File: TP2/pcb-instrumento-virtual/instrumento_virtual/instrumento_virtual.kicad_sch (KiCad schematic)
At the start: 29 parts

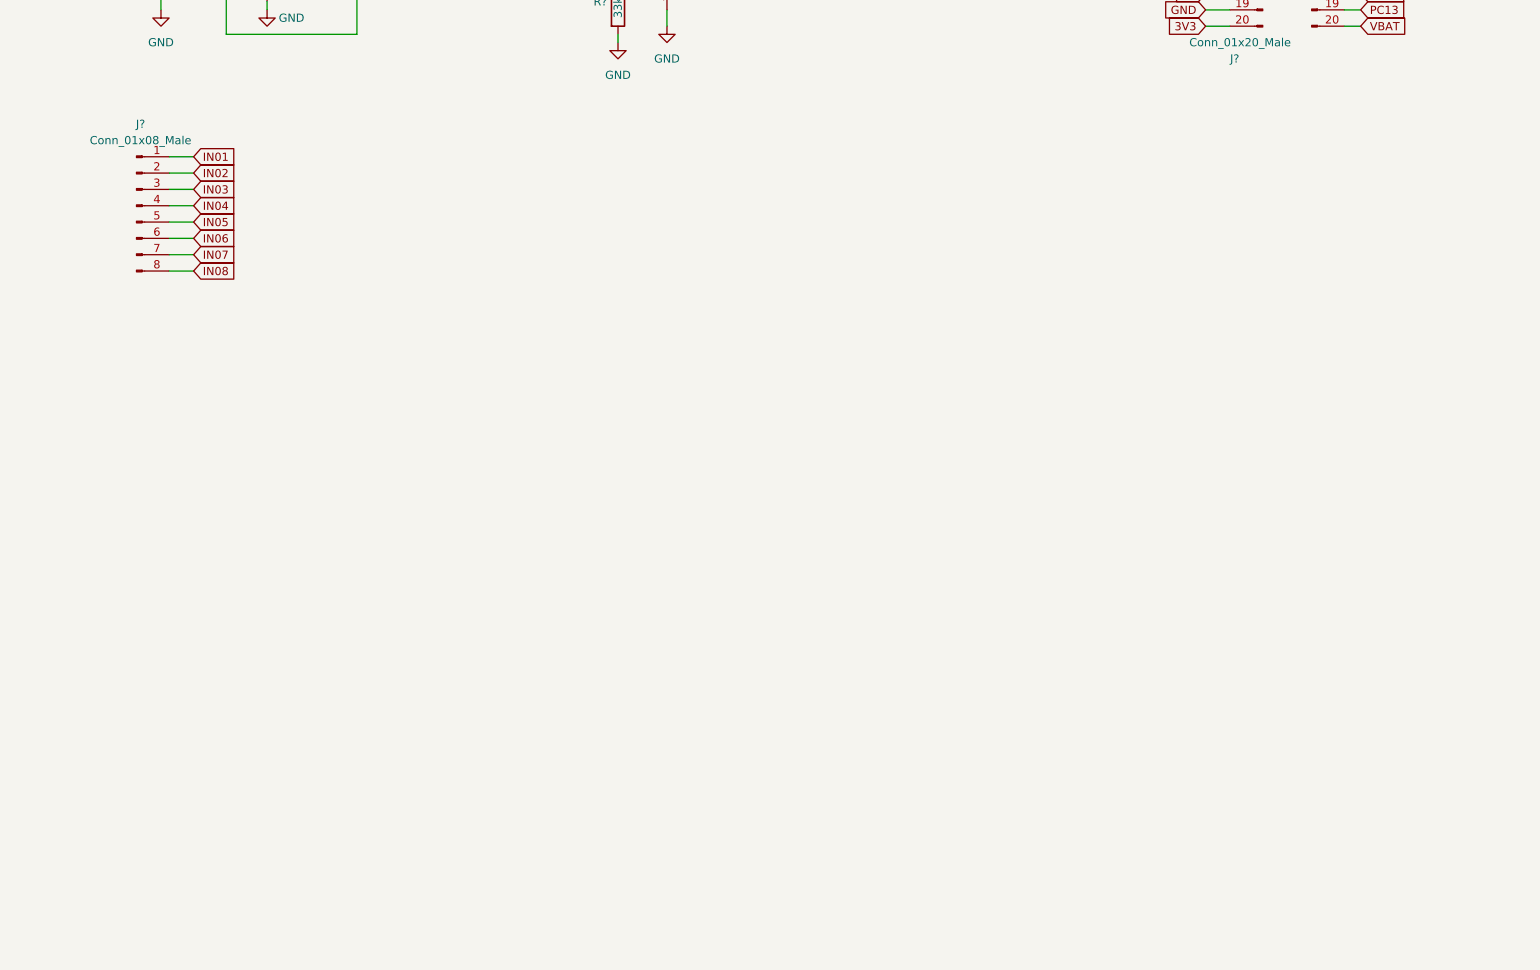
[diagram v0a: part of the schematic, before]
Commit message: agrega etapas de operacionales de entradas y circuitos de protección con clamping diodes en la pcb
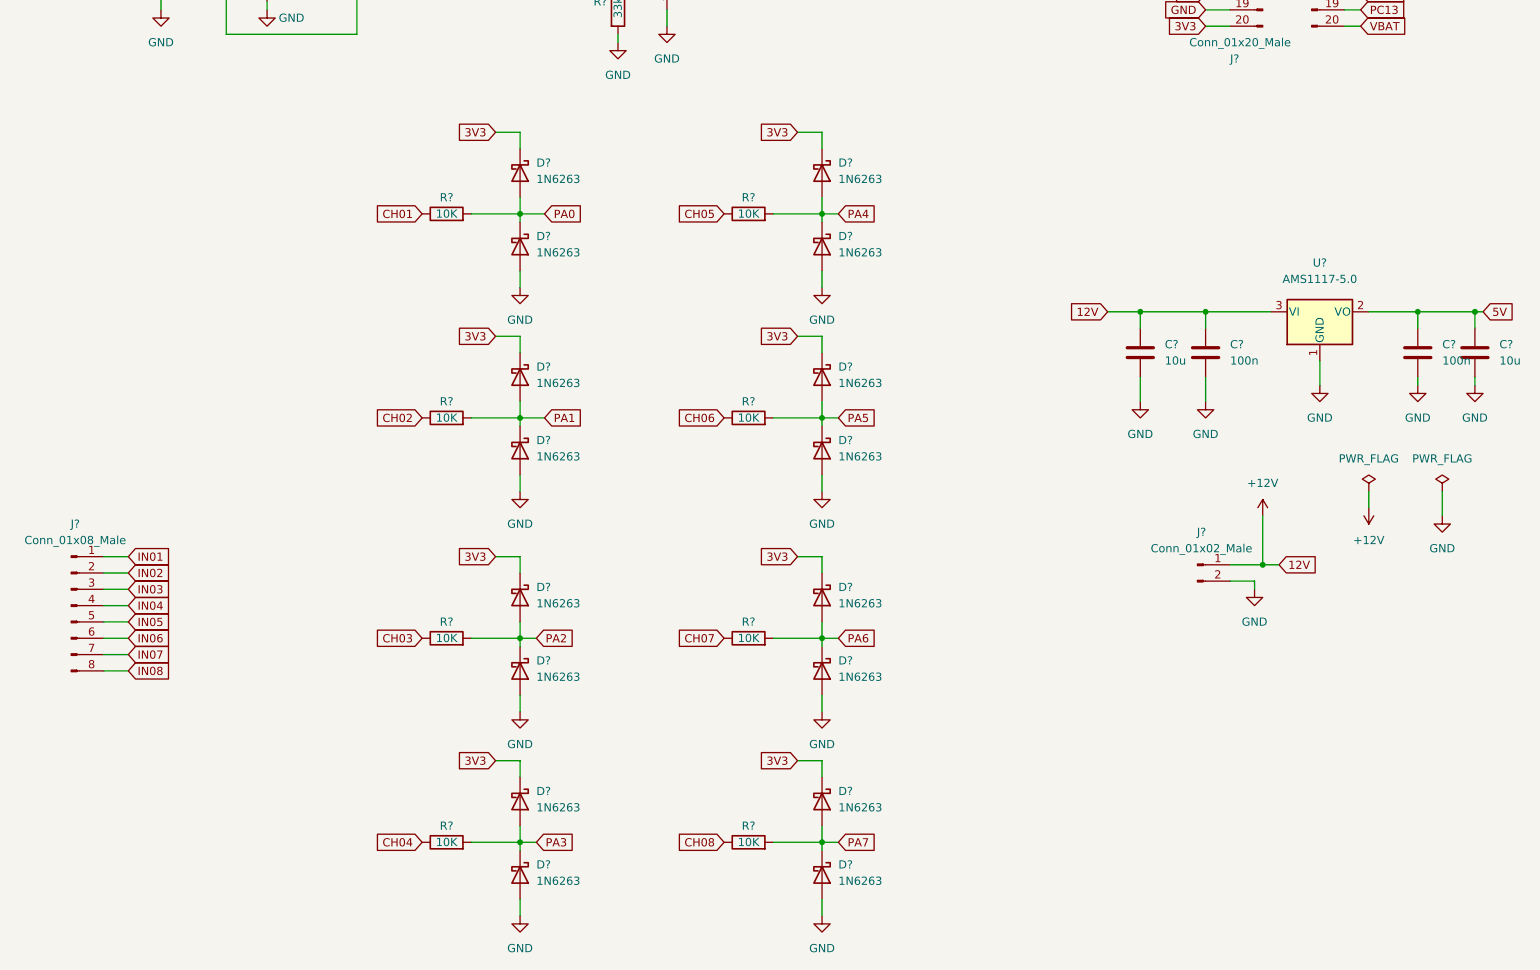
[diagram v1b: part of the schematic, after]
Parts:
- added C? (x2): 100n, symbol Device:C
- added C? (x2): 10u, symbol Device:C
- added D? (x16): 1N6263, Diode_THT:D_DO-35_SOD27_P7.62mm_Horizontal, symbol Diode:1N6263
- added J?: Conn_01x02_Male, symbol Connector:Conn_01x02_Male
- added R? (x8): 10K, symbol Device:R
- added U?: AMS1117-5.0, Package_TO_SOT_SMD:SOT-223-3_TabPin2, symbol Regulator_Linear:AMS1117-5.0
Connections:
- net 3V3: now also D?.1 (K), D?.1 (K), D?.1 (K), D?.1 (K), D?.1 (K), D?.1 (K), D?.1 (K), D?.1 (K)
- net 5V: now also C?.1, C?.1, U?.2 (VO)
- net CH01: now also R?.1
- net CH02: now also R?.1
- net CH03: now also R?.1
- net CH04: now also R?.1
- net CH05: now also R?.1
- net CH06: now also R?.1
- net CH07: now also R?.1
- net CH08: now also R?.1
- net GND: now also C?.2, C?.2, C?.2, C?.2, D?.2 (A), D?.2 (A), D?.2 (A), D?.2 (A), D?.2 (A), D?.2 (A), D?.2 (A), D?.2 (A), J?.2 (Pin_2), U?.1 (GND)
- net PA0: now also D?.1 (K), D?.2 (A), R?.2
- net PA1: now also D?.1 (K), D?.2 (A), R?.2
- net PA2: now also D?.1 (K), D?.2 (A), R?.2
- net PA3: now also D?.1 (K), D?.2 (A), R?.2
- net PA4: now also D?.1 (K), D?.2 (A), R?.2
- net PA5: now also D?.1 (K), D?.2 (A), R?.2
- net PA6: now also D?.1 (K), D?.2 (A), R?.2
- net PA7: now also D?.1 (K), D?.2 (A), R?.2
- new net +12V: C?.1, C?.1, J?.1 (Pin_1), U?.3 (VI)
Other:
- moved on the sheet: J?

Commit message: modifca pcb
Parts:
- removed D? (x12): 1N6263, Diode_THT:D_DO-35_SOD27_P7.62mm_Horizontal, symbol Diode:1N6263
- removed J? (x2): Conn_01x20_Male, symbol Connector:Conn_01x20_Male
- removed J?: Conn_01x02_Male, symbol Connector:Conn_01x02_Male
- removed J?: Conn_01x08_Male, symbol Connector:Conn_01x08_Male
- removed R? (x6): 33K, symbol Device:R
- removed R? (x6): 10K, symbol Device:R
- removed R? (x6): 68K, symbol Device:R
- removed U? (x6): MCP6001R, Package_TO_SOT_SMD:SOT-23-5, symbol Amplifier_Operational:MCP6001R
- added C5, C6: 100nF, symbol Device:C
- added J1: Conn_01x08_Socket, symbol Connector:Conn_01x08_Socket
- added J2, J4: Conn_01x02_Socket, symbol Connector:Conn_01x02_Socket
- added J3, J5: Conn_01x20_Socket, symbol Connector:Conn_01x20_Socket
- added R10, R9: 1K, symbol Device:R
- added U1: CD4051B, symbol Analog_Switch:CD4051B
- gave numbers to parts that had none: 19
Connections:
- net CH07 is gone; now on net CH01: U2.1, U2.4 (-)
- net CH08 is gone; now on net CH02: R8.1, U3.1
- net +12V: now also J4.2 (Pin_2)
- net 3V3: now also J3.3 (Pin_3), J5.20 (Pin_20)
- net 5V: now also J5.18 (Pin_18)
- net GND: now also C5.2, C6.2, J3.1 (Pin_1), J3.2 (Pin_2), J4.1 (Pin_1), J5.19 (Pin_19), U1.7 (VEE), U1.8 (VSS)
- net IN01: now also J1.8 (Pin_8), U1.13 (X0)
- net IN02: now also J1.7 (Pin_7), U1.14 (X1)
- net IN03: now also J1.6 (Pin_6), U1.15 (X2)
- net IN04: now also J1.5 (Pin_5), U1.12 (X3)
- net IN05: now also J1.4 (Pin_4), U1.1 (X4)
- net IN06: now also J1.3 (Pin_3), U1.5 (X5)
- net IN07: now also J1.2 (Pin_2), U1.2 (X6); no longer R1.1
- net IN08: now also J1.1 (Pin_1)
- net PA0: now also J3.16 (Pin_16)
- net PA1: now also J3.15 (Pin_15)
- net PA10: now also J5.7 (Pin_7)
- net PA11: now also J5.8 (Pin_8)
- net PA12: now also J5.9 (Pin_9)
- net PA15: now also J5.10 (Pin_10)
- net PA2: now also J3.14 (Pin_14)
- net PA3: now also J3.13 (Pin_13)
- net PA4: now also J3.12 (Pin_12)
- net PA5: now also J3.11 (Pin_11)
- net PA6: now also J3.10 (Pin_10)
- net PA7: now also J3.9 (Pin_9)
- net PA8: now also J5.5 (Pin_5), U1.9 (C)
- net PA9: now also J5.6 (Pin_6)
- net PB0: now also J3.8 (Pin_8)
- net PB1: now also J3.7 (Pin_7)
- net PB10: now also J3.6 (Pin_6)
- net PB11: now also J3.5 (Pin_5)
- net PB12: now also J5.1 (Pin_1)
- net PB13: now also J5.2 (Pin_2)
- net PB14: now also J5.3 (Pin_3), U1.11 (A)
- net PB15: now also J5.4 (Pin_4), U1.10 (B)
- net PB3: now also J5.11 (Pin_11)
- net PB4: now also J5.12 (Pin_12), R9.1
- net PB5: now also J5.13 (Pin_13), R10.1
- net PB6: now also J5.14 (Pin_14)
- net PB7: now also J5.15 (Pin_15)
- net PB8: now also J5.16 (Pin_16)
- net PB9: now also J5.17 (Pin_17)
- net PC13: now also J3.19 (Pin_19)
- net PC14: now also J3.18 (Pin_18)
- net PC15: now also J3.17 (Pin_17)
- net RST_BUTTON: now also J3.4 (Pin_4)
- net VBAT: now also J3.20 (Pin_20)
- new net AIN01: R1.1, U1.3 (X)
- new net AOUT01: C5.1, J2.1 (Pin_1), R9.2
- new net AOUT02: C6.1, J2.2 (Pin_2), R10.2
- new net VDD: U1.16 (VDD)
- no-connect marks 0 -> 2
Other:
- moved on the sheet: D1, D2, D3, D4, R1, R2, R6, R7, U2

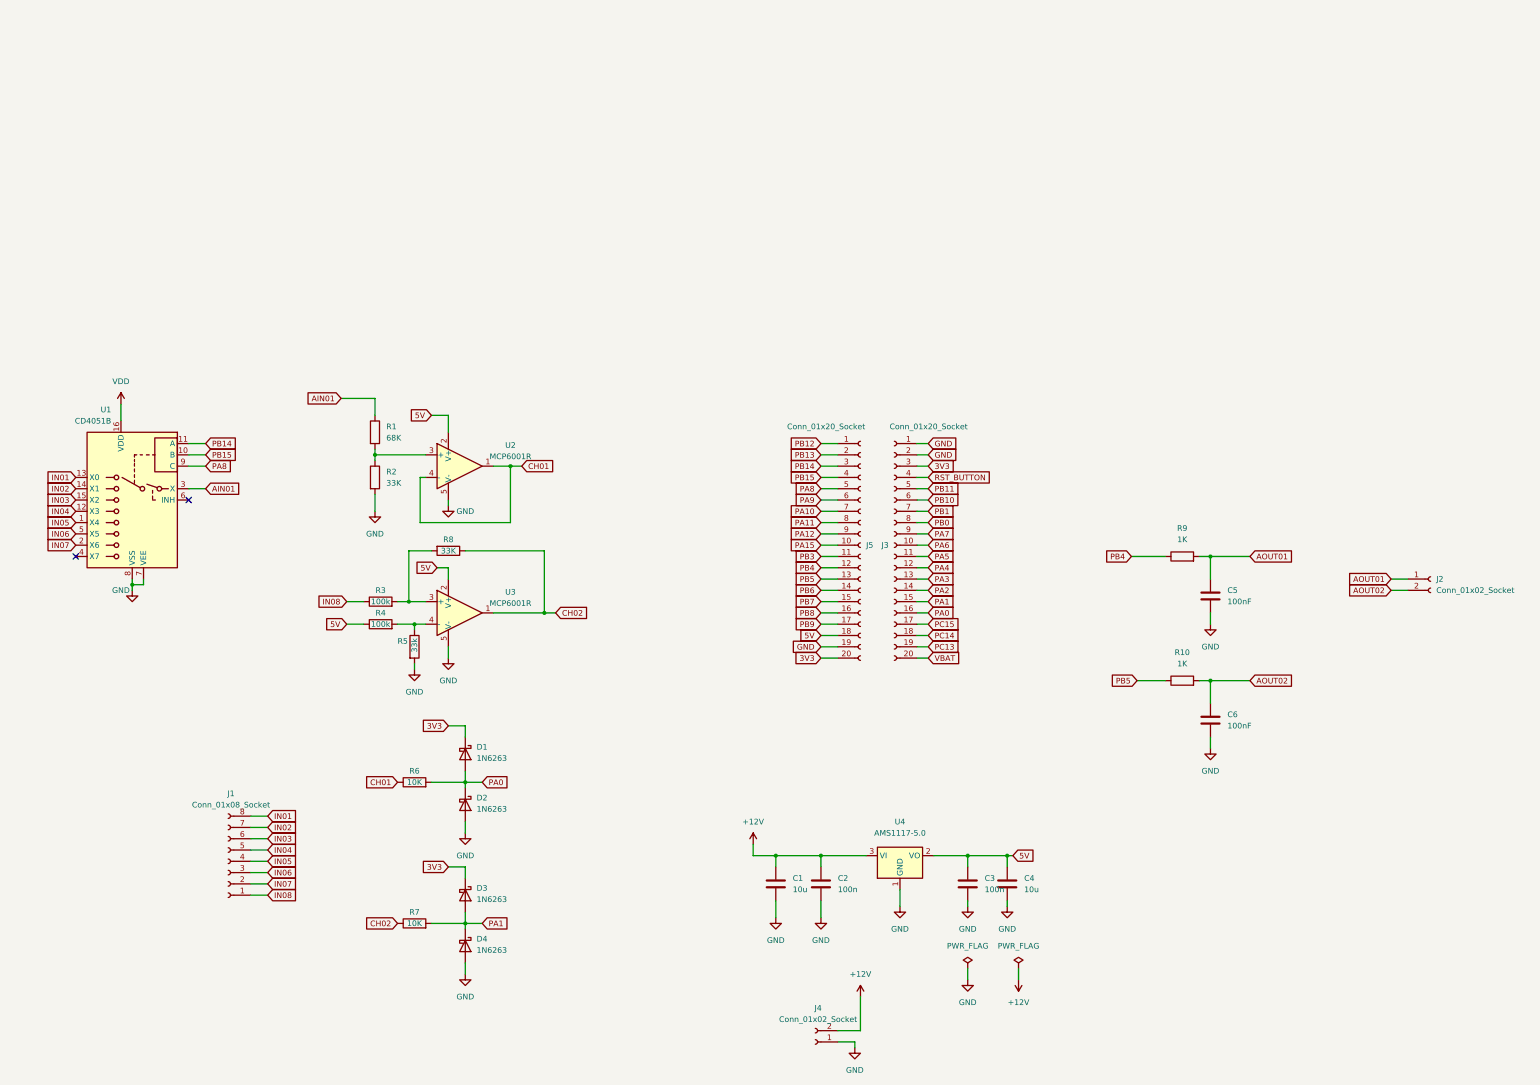
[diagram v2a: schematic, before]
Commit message: Version de pcb con regulación de 5v
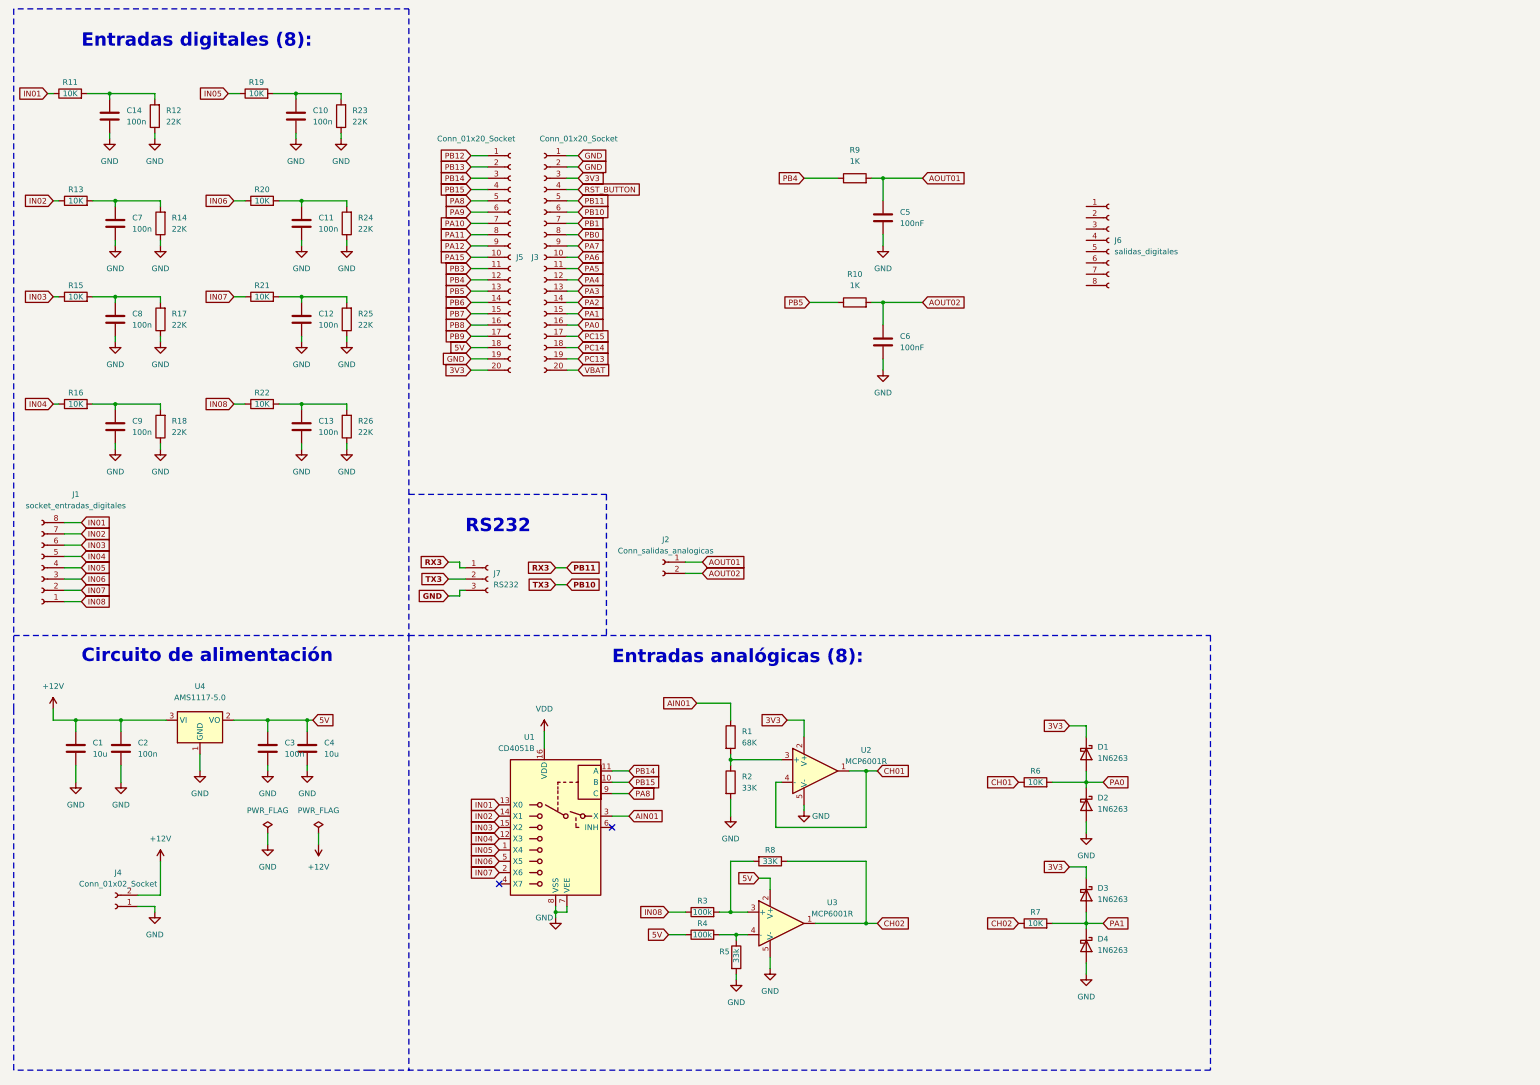
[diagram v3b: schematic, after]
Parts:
- added C10, C11, C12, C13, C14, C7, C8, C9: 100n, symbol Device:C
- added J6: salidas_digitales, symbol Connector:Conn_01x08_Socket
- added J7: RS232, symbol Connector:Conn_01x03_Socket
- added R11, R13, R15, R16, R19, R20, R21, R22: 10K, symbol Device:R
- added R12, R14, R17, R18, R23, R24, R25, R26: 22K, symbol Device:R
- J1: value Conn_01x08_Socket -> socket_entradas_digitales
- J2: value Conn_01x02_Socket -> Conn_salidas_analogicas
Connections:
- net 3V3: now also U2.2 (V+)
- net 5V: no longer U2.2 (V+)
- net GND: now also C10.2, C11.2, C12.2, C13.2, C14.2, C7.2, C8.2, C9.2, J7.3 (Pin_3), R12.1, R14.1, R17.1, R18.1, R23.1, R24.1, R25.1, R26.1
- net IN01: now also R11.1
- net IN02: now also R13.1
- net IN03: now also R15.1
- net IN04: now also R16.1
- net IN05: now also R19.1
- net IN06: now also R20.1
- net IN07: now also R21.1
- net IN08: now also R22.1
- net PB10: now also J7.2 (Pin_2)
- net PB11: now also J7.1 (Pin_1)
- new net: C10.1, R19.2, R23.2
- new net: C7.1, R13.2, R14.2
- new net: C12.1, R21.2, R25.2
- new net: C8.1, R15.2, R17.2
- new net: C14.1, R11.2, R12.2
- new net: C13.1, R22.2, R26.2
- new net: C9.1, R16.2, R18.2
- new net: C11.1, R20.2, R24.2
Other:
- note added: "Circuito de alimentación"
- note added: "Entradas analógicas (8):"
- note added: "Entradas digitales (8):"
- note added: "RS232"
- moved on the sheet: C1, C2, C3, C4, C5, C6, D1, D2, D3, D4, J1, J2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
